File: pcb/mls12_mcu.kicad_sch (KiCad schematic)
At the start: 35 parts, among them J2 TC2070-FP, J3 SM04B-SRSS-TB, U3 STM32H563RIT6, Y2 25MHz

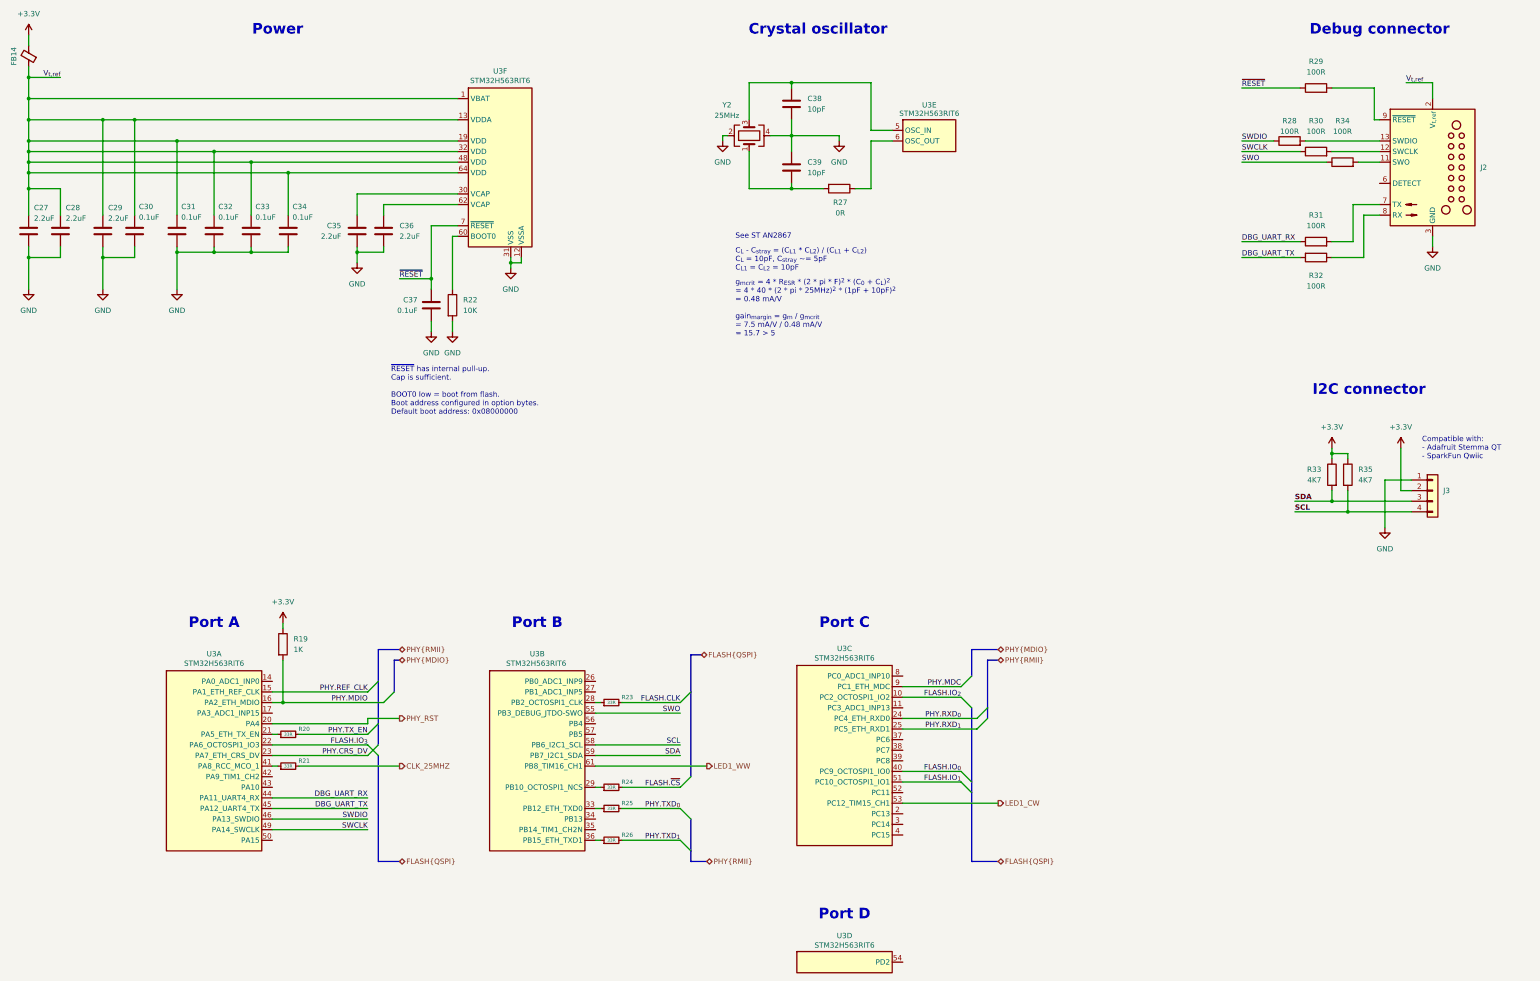
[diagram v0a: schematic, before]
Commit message: Update to 25W PoE+ module, 2 outputs
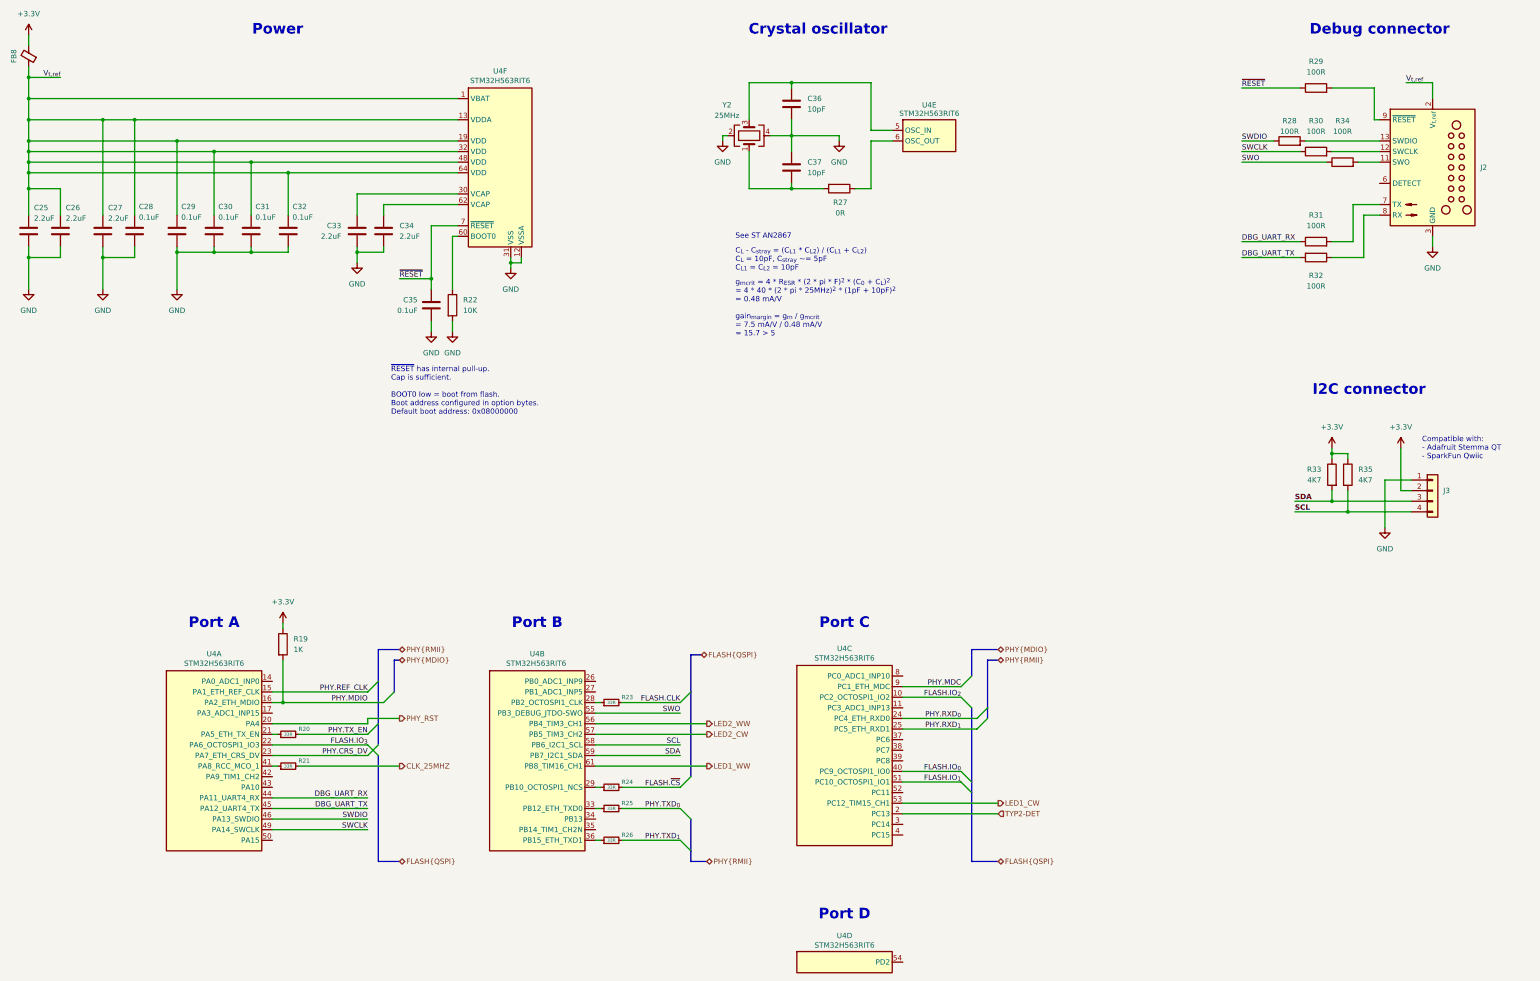
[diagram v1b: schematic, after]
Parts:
- renumbered C27 to C25, C28 to C26, C29 to C27, C30 to C28, C31 to C29, C32 to C30, C33 to C31, C34 to C32, C35 to C33, C36 to C34, C37 to C35, C38 to C36, C39 to C37, FB14 to FB8, U3 to U4
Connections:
- net LED2_WW: now reaches U4.56 (PB4)
- net LED2_CW: now reaches U4.57 (PB5)
- net TYP2-DET: now reaches U4.2 (PC13)
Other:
- company: (none) -> Quomodo BV

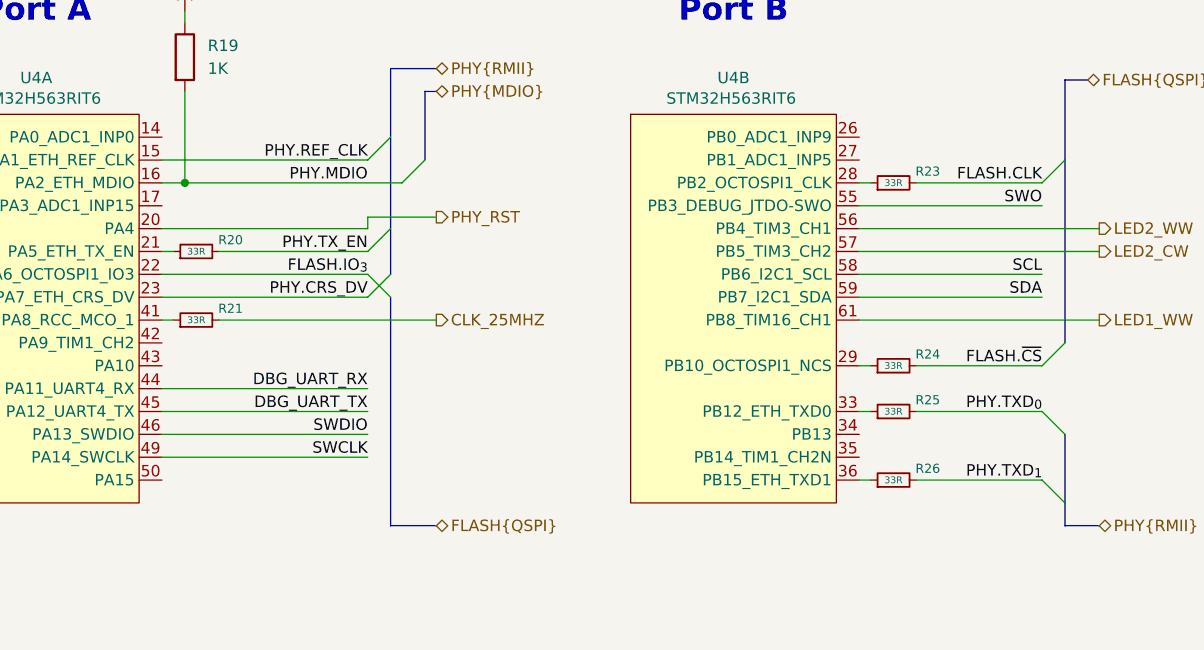
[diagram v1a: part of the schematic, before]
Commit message: Initial RMII, MDIO routing
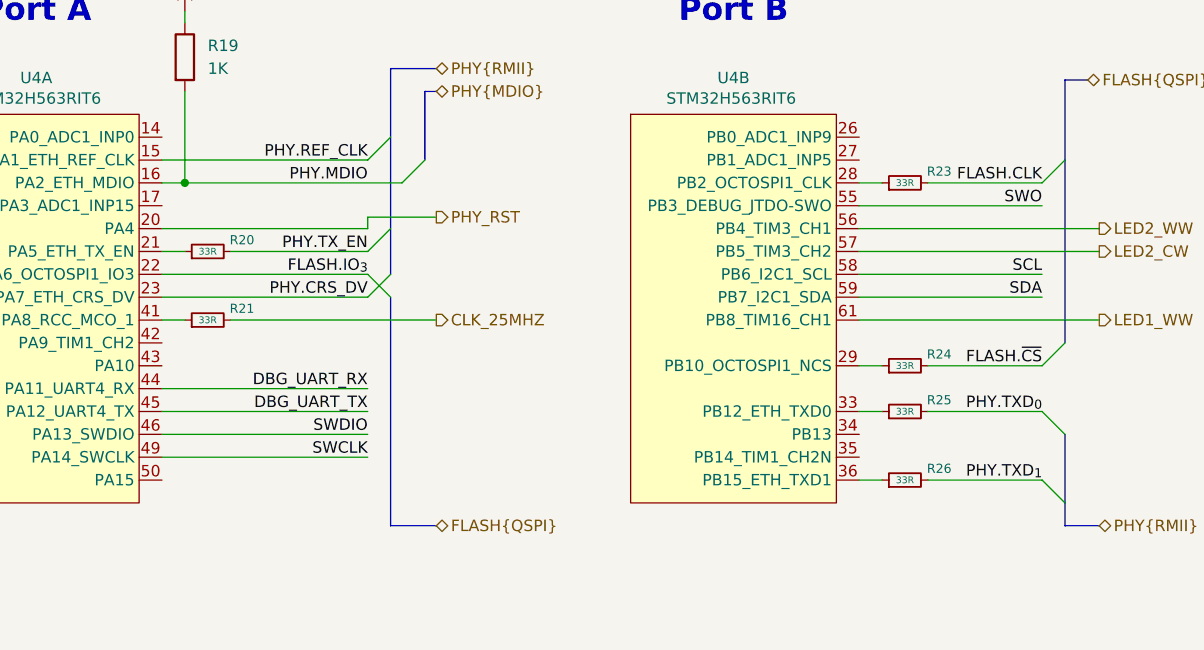
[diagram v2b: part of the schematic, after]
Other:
- moved on the sheet: R20, R21, R23, R24, R25, R26
